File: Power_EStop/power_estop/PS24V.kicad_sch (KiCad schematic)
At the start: 0 parts

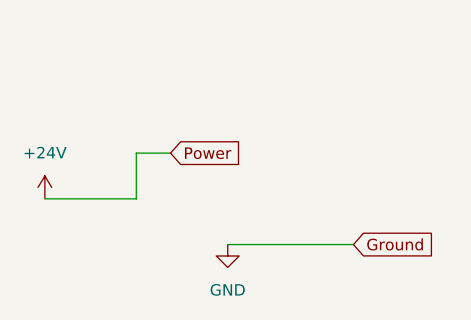
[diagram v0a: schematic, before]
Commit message: added some of stm32 power sources
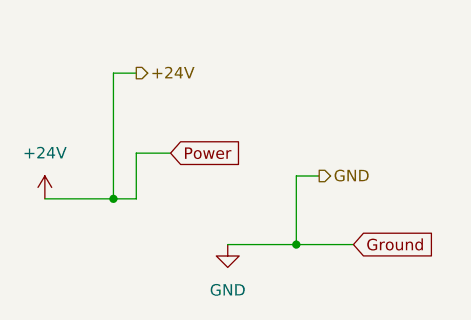
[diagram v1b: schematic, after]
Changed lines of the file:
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@@
 	(generator_version "9.0")
 	(paper "A4")
+	(junction
+		(at 67.31 86.36)
+		(diameter 0)
+		(color 0 0 0 0)
+	)
+	(junction
+		(at 87.63 91.44)
+		(diameter 0)
+		(color 0 0 0 0)
+	)
+	(wire
+		(pts
+			(xy 67.31 72.39) (xy 67.31 86.36)
+		)
+		(stroke
+			(width 0)
+			(type default)
+		)
+	)
 	(wire
 		(pts
@@
 	(wire
 		(pts
-			(xy 59.69 86.36) (xy 69.85 86.36)
+			(xy 87.63 83.82) (xy 87.63 91.44)
+		)
+		(stroke
+			(width 0)
+			(type default)
+		)
+	)
+	(wire
+		(pts
+			(xy 87.63 91.44) (xy 93.98 91.44)
+		)
+		(stroke
+			(width 0)
+			(type default)
+		)
+	)
+	(wire
+		(pts
+			(xy 90.17 83.82) (xy 87.63 83.82)
+		)
+		(stroke
+			(width 0)
+			(type default)
+		)
+	)
+	(wire
+		(pts
+			(xy 59.69 86.36) (xy 67.31 86.36)
+		)
+		(stroke
+			(width 0)
+			(type default)
+		)
+	)
+	(wire
+		(pts
+			(xy 69.85 72.39) (xy 67.31 72.39)
+		)
+		(stroke
+			(width 0)
+			(type default)
+		)
+	)
+	(wire
+		(pts
+			(xy 67.31 86.36) (xy 69.85 86.36)
 		)
 		(stroke
@@
 	(wire
 		(pts
-			(xy 80.01 91.44) (xy 93.98 91.44)
+			(xy 80.01 91.44) (xy 87.63 91.44)
 		)
 		(stroke
@@
 		)
 	)
+	(hierarchical_label "GND"
+		(shape output)
+		(at 90.17 83.82 0)
+		(effects
+			(font
+				(size 1.27 1.27)
+			)
+			(justify left)
+		)
+	)
+	(hierarchical_label "+24V"
+		(shape output)
+		(at 69.85 72.39 0)
+		(effects
+			(font
+				(size 1.27 1.27)
+			)
+			(justify left)
+		)
+	)

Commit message: added solid state relay foot print
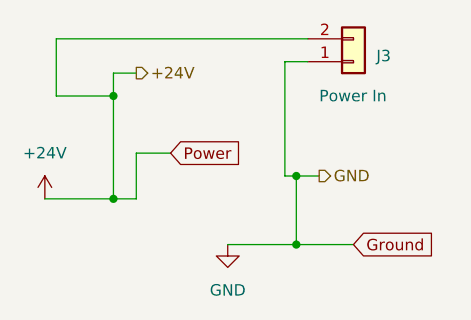
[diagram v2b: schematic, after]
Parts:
- added J3: Power In, Connector_AMASS:AMASS_XT60-M_1x02_P7.20mm_Vertical, symbol Connector_Generic:Conn_01x02
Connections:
- net +24V: now also J3.2 (Pin_2)
- net GND: now also J3.1 (Pin_1)
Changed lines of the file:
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@@
 		(color 0 0 0 0)
 	)
-	(wire
-		(pts
-			(xy 67.31 72.39) (xy 67.31 86.36)
+	(junction
+		(at 87.63 83.82)
+		(diameter 0)
+		(color 0 0 0 0)
+	)
+	(junction
+		(at 67.31 74.93)
+		(diameter 0)
+		(color 0 0 0 0)
+	)
+	(wire
+		(pts
+			(xy 67.31 72.39) (xy 67.31 74.93)
+		)
+		(stroke
+			(width 0)
+			(type default)
+		)
+	)
+	(wire
+		(pts
+			(xy 60.96 74.93) (xy 67.31 74.93)
 		)
 		(stroke
@@
 	(wire
 		(pts
+			(xy 88.9 71.12) (xy 86.36 71.12)
+		)
+		(stroke
+			(width 0)
+			(type default)
+		)
+	)
+	(wire
+		(pts
+			(xy 86.36 71.12) (xy 86.36 83.82)
+		)
+		(stroke
+			(width 0)
+			(type default)
+		)
+	)
+	(wire
+		(pts
 			(xy 69.85 81.28) (xy 69.85 86.36)
 		)
@@
 	(wire
 		(pts
+			(xy 86.36 83.82) (xy 87.63 83.82)
+		)
+		(stroke
+			(width 0)
+			(type default)
+		)
+	)
+	(wire
+		(pts
+			(xy 60.96 68.58) (xy 60.96 74.93)
+		)
+		(stroke
+			(width 0)
+			(type default)
+		)
+	)
+	(wire
+		(pts
+			(xy 67.31 74.93) (xy 67.31 86.36)
+		)
+		(stroke
+			(width 0)
+			(type default)
+		)
+	)
+	(wire
+		(pts
 			(xy 80.01 91.44) (xy 87.63 91.44)
+		)
+		(stroke
+			(width 0)
+			(type default)
+		)
+	)
+	(wire
+		(pts
+			(xy 88.9 68.58) (xy 60.96 68.58)
 		)
 		(stroke
@@
 					(unit 1)
 				)
+			)
+		)
+	)
+	(symbol
+		(lib_id "Connector_Generic:Conn_01x02")
+		(at 93.98 71.12 0)
+		(mirror x)
+		(unit 1)
+		(exclude_from_sim no)
+		(in_bom yes)
+		(on_board yes)
+		(dnp no)
+		(property "Reference" "J3"
+			(at 96.52 70.485 0)
+			(effects
+				(font
+					(size 1.27 1.27)
+				)
+				(justify left)
+			)
+		)
+		(property "Value" "Power In"
+			(at 90.17 74.93 0)
+			(effects
+				(font
+					(size 1.27 1.27)
+				)
+				(justify left)
+			)
+		)
+		(property "Footprint" "Connector_AMASS:AMASS_XT60-M_1x02_P7.20mm_Vertical"
+			(at 93.98 71.12 0)
+			(effects
+				(font
+					(size 1.27 1.27)
+				)
+				(hide yes)
+			)
+		)
+		(property "Datasheet" "~"
+			(at 93.98 71.12 0)
+			(effects
+				(font
+					(size 1.27 1.27)
+				)
+				(hide yes)
+			)
+		)
+		(property "Description" "Generic connector, single row, 01x02, script generated (kicad-library-utils/schlib/autogen/connector/)"
+			(at 93.98 71.12 0)
+			(effects
+				(font
+					(size 1.27 1.27)
+				)
+				(hide yes)
+			)
+		)
+		(pin "1"
+		)
+		(pin "2"
+		)
+		(instances
+			(project "power_estop"
+				(path "/03a0e3dc-ea94-451b-93a3-0e9375a73668/20fa2568-a808-4634-926f-bb7bea31986c"
+					(reference "J3")
+					(unit 1)
+				)
